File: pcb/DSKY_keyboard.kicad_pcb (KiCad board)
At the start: 2 copper layers, 170.2 x 81.9 mm, 62 parts, among them CN1 4U#20329, IC1 ATSAMD21E, J1 MOUNTINGHOLE3.0, J2 MOUNTINGHOLE3.0, J6 MOUNTINGHOLE3.0, J8 MOUNTINGHOLE3.0, Q1 reset, U1 AP2112K-3.3, U2 AQY232SZ

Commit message: Revised the board outline to eliminate two mechanical clearance issues
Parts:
- moved Q1 60.9 mm to (164.6, 71.8)
- moved IC1 56.8 mm to (165.1, 89.9)
- moved C1 56.7 mm to (164.2, 80.4)
- moved R10 54.9 mm to (138.4, 84.7)
- moved U2 54.9 mm to (140.6, 90.6)
- moved C2 53.0 mm to (171.6, 86.6), turned to 180 degrees
- moved R1 44.7 mm to (187.9, 89.7)
- moved U1 44.1 mm to (176.6, 89.8)
- moved PWR1 41.6 mm to (188.1, 87.4)
- moved CN1 39.4 mm to (177.0, 70.4)
- moved JP2 39.2 mm to (140.1, 75.1)
- moved C3 29.3 mm to (180.3, 86.6), turned to 0 degrees
- moved D2 26.0 mm to (188.0, 82.5)
- moved J1 25.9 mm to (115.4, 80.8)
- moved J2 25.3 mm to (115.4, 128.8)
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- renumbered REF** to REF1
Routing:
- net PA28: track 157.5 -> 70.8 mm
- net PA07: track 162.2 -> 82.3 mm, vias 0 -> 3
- net PA17: track 85.8 -> 21.5 mm
- net PA19: track 104.3 -> 45.6 mm, vias 0 -> 1
- net PA22: track 111.4 -> 58.1 mm, vias 0 -> 1
- net PA06: track 26.3 -> 79.2 mm, vias 1 -> 2
- net PA23: track 123.0 -> 71.7 mm, vias 1 -> 2
- net PA16: track 72.0 -> 20.7 mm, vias 0 -> 1
- net PA11: track 156.1 -> 106.5 mm
- net PA02: track 16.9 -> 66.4 mm
- net PA27: track 159.4 -> 111.3 mm
- net GND: track 604.9 -> 557.2 mm
- net /D2_A1_PA09_SCL_MISO: track 31.6 -> 74.0 mm
- net PA01: track 53.8 -> 88.8 mm, vias 1 -> 0
- net PA14: track 53.1 -> 21.0 mm
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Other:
- board size 170.2 x 81.9 mm -> 170.2 x 71.1 mm

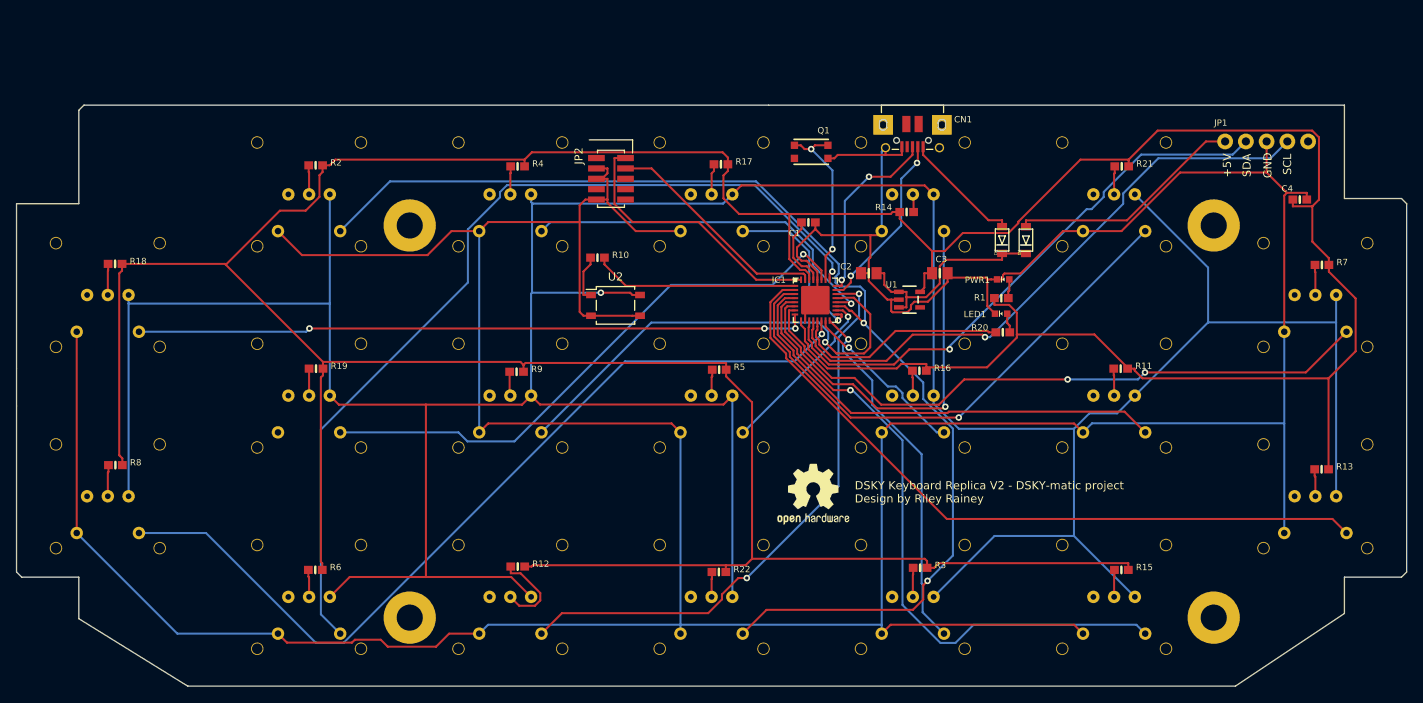
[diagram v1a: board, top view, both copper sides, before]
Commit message: Issue #1
Board now has (CLR) on PA00; backlighting always on. V3 board
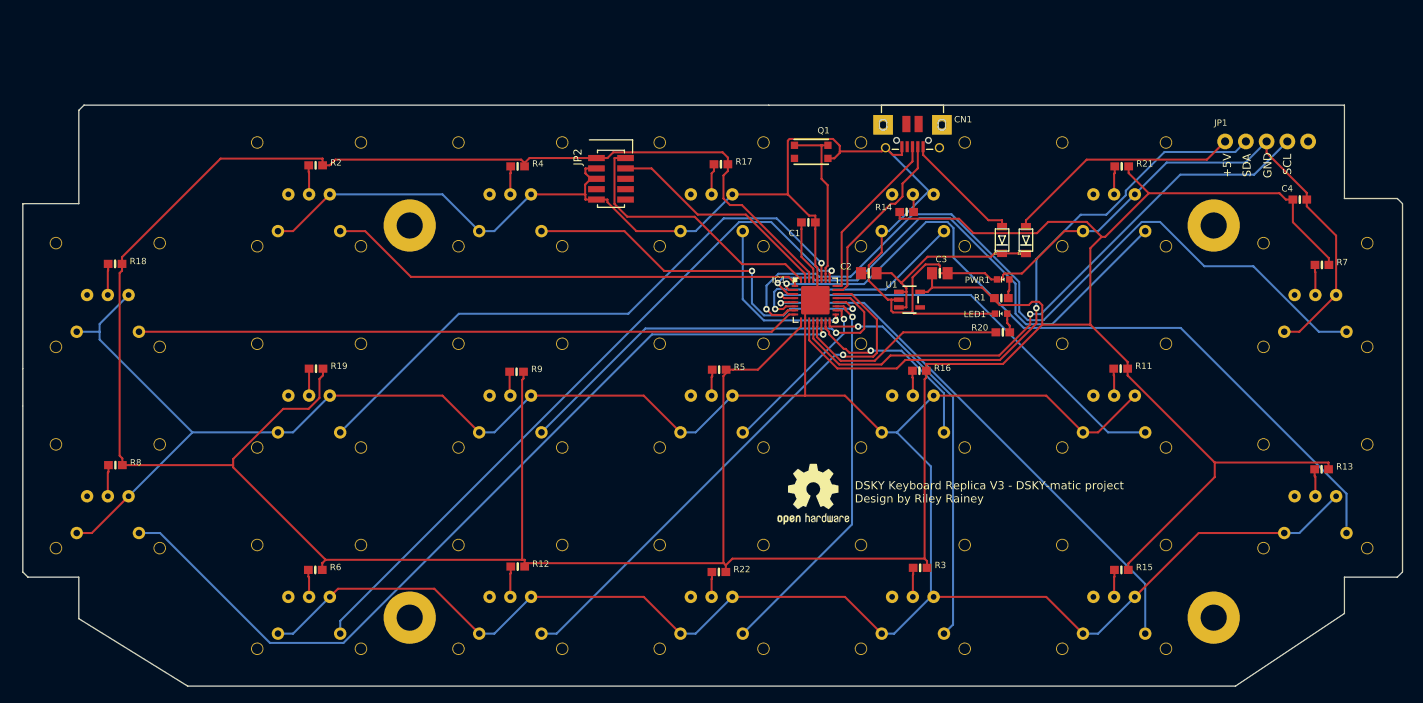
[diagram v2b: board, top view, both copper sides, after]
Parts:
- removed R10: 1.1K, Trinket M0 rev D:0603-NO
- removed U2: AQY232SZ, Package_SO:SO-4_4.4x4.3mm_P2.54mm
- D1, D2: value SCHOTTKY -> SCHOTTKY 30V
- JP2: value 20021221-00010C4LF -> 3221-10-0300-00-TR
- R1: value 10K -> 1.5K
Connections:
- JP2 pad 1: +3V3 -> 3.3V
- S1 pad 1: Net-(S1-Pad1) -> GND
- S1 pad 3: Net-(S1-Pad3) -> GND
- S10 pad 3: Net-(S1-Pad3) -> GND
- S11 pad 3: Net-(S1-Pad3) -> GND
- S12 pad 3: Net-(S1-Pad3) -> GND
- S13 pad 3: Net-(S1-Pad3) -> GND
- S14 pad 3: Net-(S1-Pad3) -> GND
- S15 pad 3: Net-(S1-Pad3) -> GND
- S16 pad 3: Net-(S1-Pad3) -> GND
- S17 pad 3: Net-(S1-Pad3) -> GND
- S18 pad 3: Net-(S1-Pad3) -> GND
- S19 pad 3: Net-(S1-Pad3) -> GND
- S2 pad 3: Net-(S1-Pad3) -> GND
- S3 pad 3: Net-(S1-Pad3) -> GND
- S4 pad 3: Net-(S1-Pad3) -> GND
- S5 pad 3: Net-(S1-Pad3) -> GND
- S6 pad 2: PA18 -> PA00
- S6 pad 3: Net-(S1-Pad3) -> GND
- S7 pad 3: Net-(S1-Pad3) -> GND
- S8 pad 3: Net-(S1-Pad3) -> GND
- S9 pad 3: Net-(S1-Pad3) -> GND
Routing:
- net Net-(S1-Pad3): track 455.5 -> 0.00 mm, vias 1 -> 0
- net PA18: track 146.1 -> 47.1 mm, vias 2 -> 1
- net GND: track 557.2 -> 611.7 mm
- net PA00: track 25.2 -> 58.6 mm
- net PA27: track 111.3 -> 85.6 mm
- net 3.3V: track 536.1 -> 514.3 mm
- net PA05: track 49.7 -> 28.6 mm
- net PA06: track 79.2 -> 99.9 mm, vias 2 -> 1
- net PA04: track 78.9 -> 66.7 mm
- net Net-(R12-Pad1): track 10.7 -> 3.74 mm
- net PA22: track 58.1 -> 51.5 mm
- net Net-(R10-Pad1): track 5.86 -> 0.00 mm
- net PA23: track 71.7 -> 65.9 mm, vias 2 -> 1
- net PA01: track 88.8 -> 94.1 mm, vias 0 -> 1
- net /D0_A4_PA08_SDA: track 69.4 -> 73.8 mm
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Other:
- board size 170.2 x 71.1 mm -> 168.9 x 71.1 mm
- board text added: "DSKY Keyboard Replica V3 - DSKY-matic project Design by Riley Rainey"
- board text added: "DSKY Keyboard Replica V3 -DSKY-matic project Design by Riley Rainey"
- board text removed: "DSKY Keyboard Replica V2 - DSKY-matic project Design by Riley Rainey"
- board text removed: "DSKY Keyboard Replica V2 -DSKY-matic project Design by Riley Rainey"

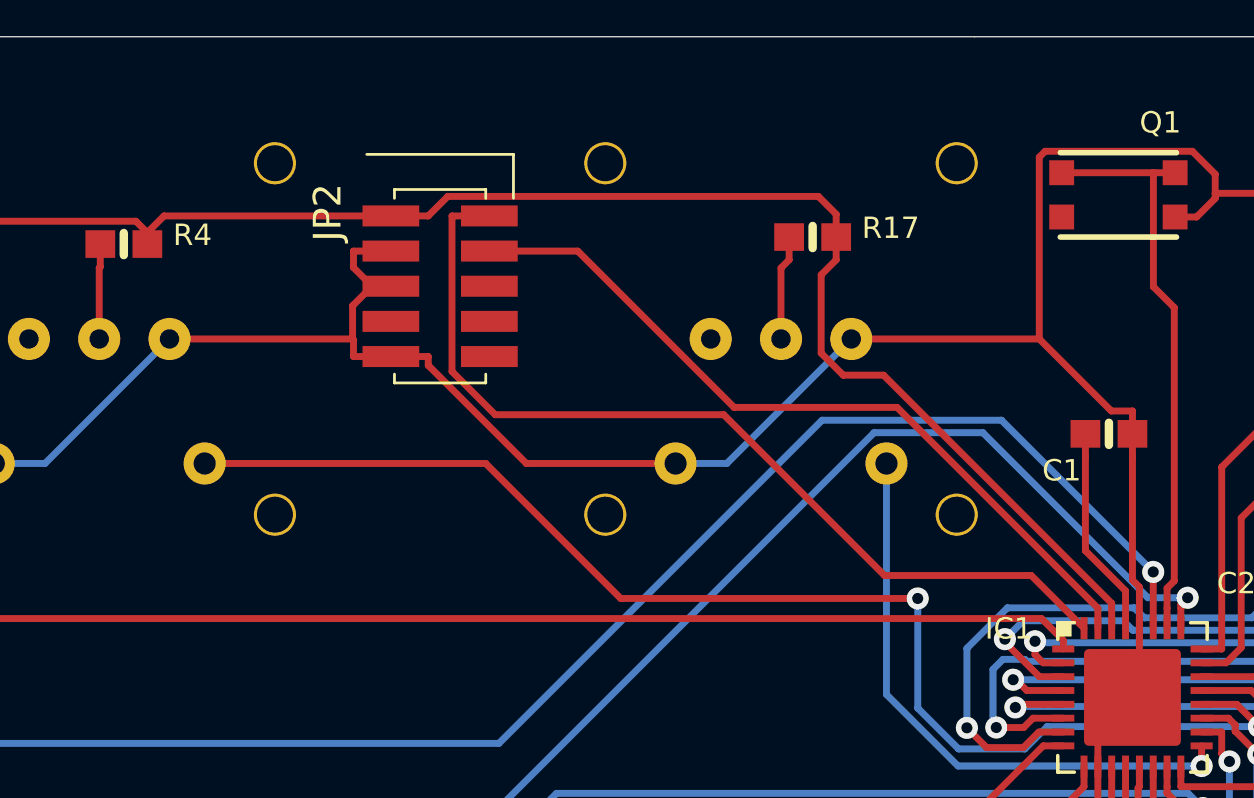
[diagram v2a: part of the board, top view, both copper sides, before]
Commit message: Update J-Link Header PCB Footprint
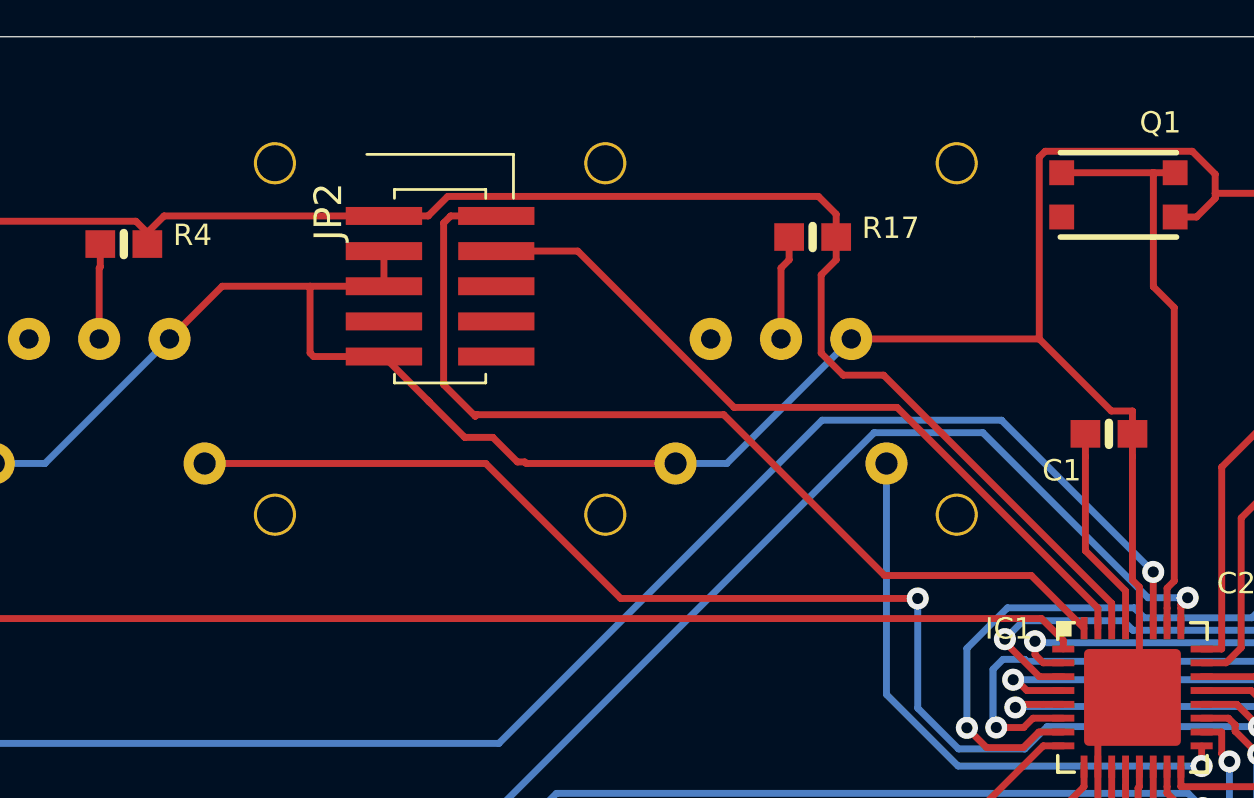
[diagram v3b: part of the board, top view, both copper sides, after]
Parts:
- JP2: footprint Trinket M0 rev D:20021221-00010C4LF -> Trinket M0 rev D:3221-10-0300-00-TR
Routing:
- net GND: track 611.7 -> 615.8 mm
- net /SWDIO: track 33.7 -> 34.4 mm

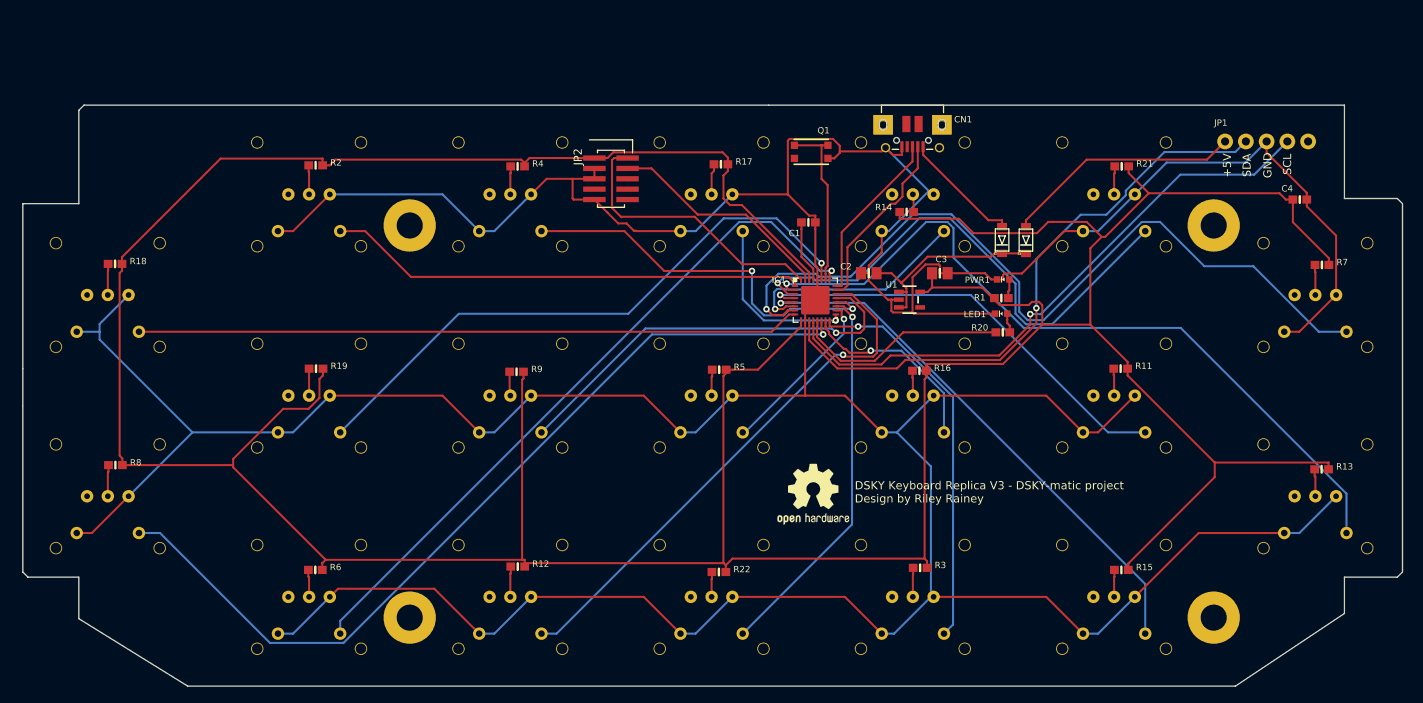
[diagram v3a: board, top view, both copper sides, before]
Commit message: V2 Board complete
V3 updates subsequent to full-up V2 board tests (incl. firmware)
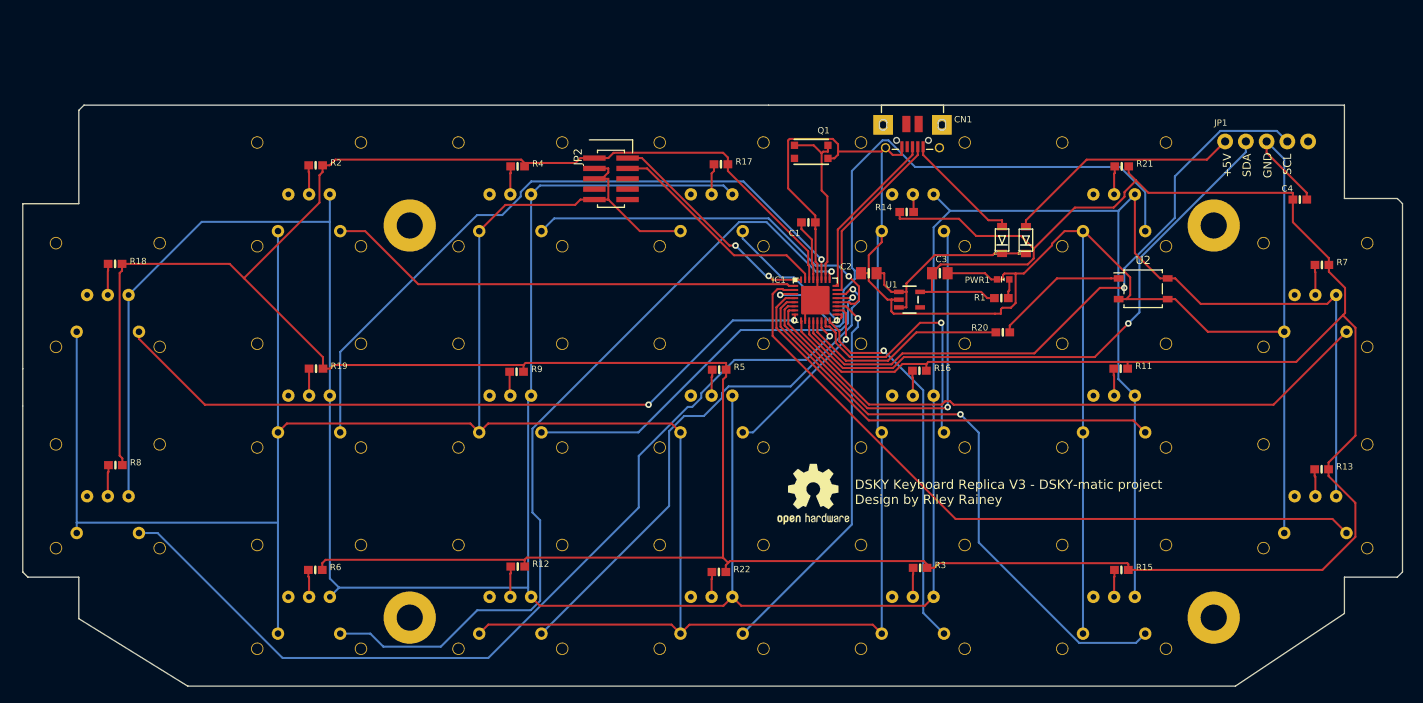
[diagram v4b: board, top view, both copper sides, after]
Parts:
- removed LED1: red, Trinket M0 rev D:CHIPLED_0603_NOOUTLINE
- added U2: AQY232SZ, Package_SO:SO-4_4.4x4.3mm_P2.54mm, F.Cu at (205.2, 88.5)
- R20: value 1.5K -> 1.1K
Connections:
- S1 pad 3: GND -> Net-(S1-Pad3)
- S10 pad 3: GND -> Net-(S1-Pad3)
- S11 pad 3: GND -> Net-(S1-Pad3)
- S12 pad 3: GND -> Net-(S1-Pad3)
- S13 pad 3: GND -> Net-(S1-Pad3)
- S14 pad 3: GND -> Net-(S1-Pad3)
- S15 pad 3: GND -> Net-(S1-Pad3)
- S16 pad 3: GND -> Net-(S1-Pad3)
- S17 pad 3: GND -> Net-(S1-Pad3)
- S18 pad 3: GND -> Net-(S1-Pad3)
- S19 pad 3: GND -> Net-(S1-Pad3)
- S2 pad 3: GND -> Net-(S1-Pad3)
- S3 pad 3: GND -> Net-(S1-Pad3)
- S4 pad 3: GND -> Net-(S1-Pad3)
- S5 pad 3: GND -> Net-(S1-Pad3)
- S6 pad 3: GND -> Net-(S1-Pad3)
- S7 pad 3: GND -> Net-(S1-Pad3)
- S8 pad 3: GND -> Net-(S1-Pad3)
- S9 pad 3: GND -> Net-(S1-Pad3)
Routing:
- net Net-(S1-Pad3): track 0.00 -> 459.2 mm
- net 3.3V: track 514.3 -> 557.3 mm
- net GND: track 615.8 -> 581.8 mm
- net PA06: track 99.9 -> 78.9 mm, vias 1 -> 0
- net PA05: track 28.6 -> 49.3 mm
- net Net-(R20-Pad1): track 2.41 -> 16.6 mm
- net PA27: track 85.6 -> 99.6 mm
- net PA02: track 63.6 -> 75.5 mm
- net PA28: track 74.1 -> 84.2 mm
- net PA14: track 23.9 -> 32.5 mm
- net PA07: track 81.2 -> 89.5 mm, vias 0 -> 2
- net /SWDIO: track 34.4 -> 27.4 mm, vias 0 -> 2
- net PA11: track 106.8 -> 113.6 mm
- net PA04: track 66.7 -> 73.3 mm
- net PA01: track 94.1 -> 88.4 mm, vias 1 -> 0
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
